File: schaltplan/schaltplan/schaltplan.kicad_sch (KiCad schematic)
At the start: 14 parts, among them SW1 SW_Nidec_CAS-120A1, U1 DFR0478

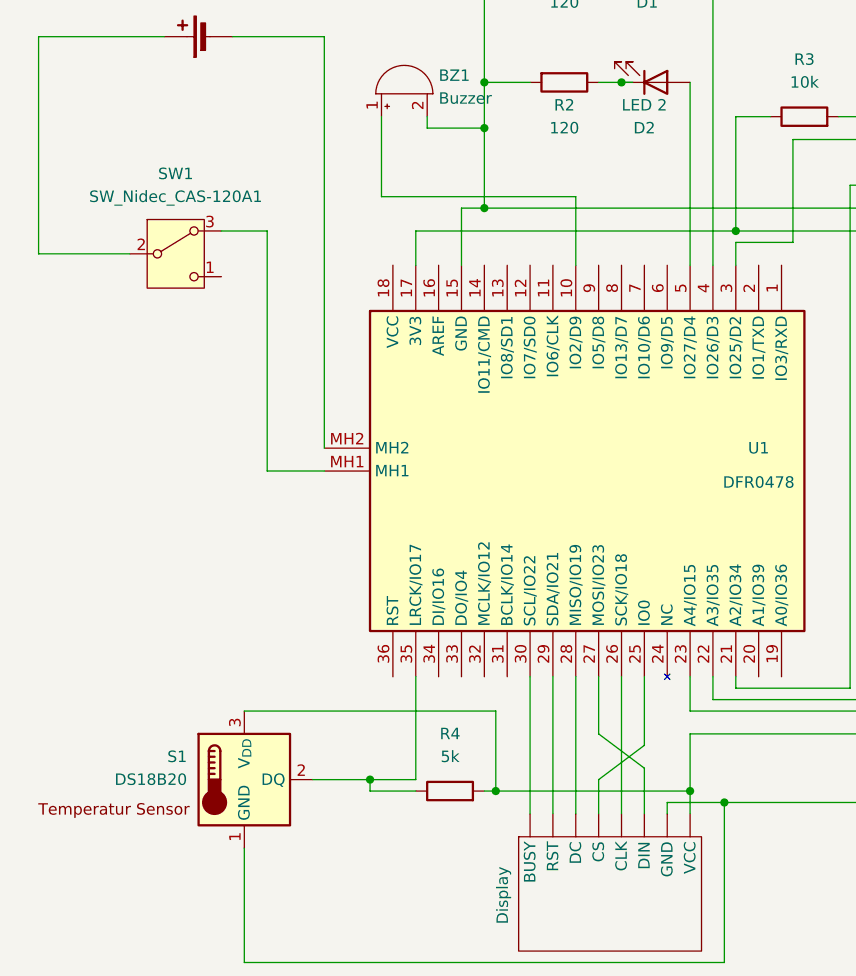
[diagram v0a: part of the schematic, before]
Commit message: schaltplan farbiger gemacht
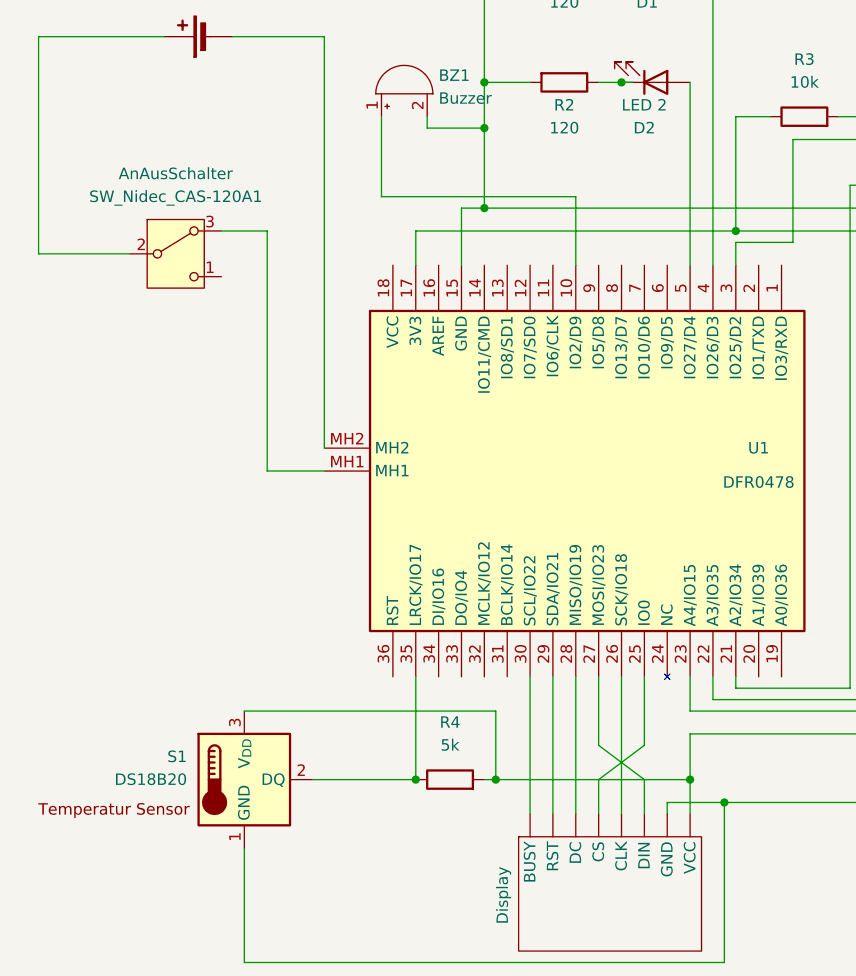
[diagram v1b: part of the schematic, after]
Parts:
- renumbered SW1 to AnAusSchalter
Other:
- moved on the sheet: R4
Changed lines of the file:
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@@
 	)
 	(junction
-		(at 90.17 134.62)
+		(at 68.58 133.35)
 		(diameter 0)
 		(color 0 0 0 0)
@@
 	)
 	(junction
+		(at 90.17 133.35)
+		(diameter 0)
+		(color 0 0 0 0)
+	)
+	(junction
 		(at 120.65 72.39)
 		(diameter 0)
@@
 	)
 	(junction
-		(at 93.98 135.89)
+		(at 59.69 133.35)
 		(diameter 0)
 		(color 0 0 0 0)
 	)
 	(junction
-		(at 54.61 133.35)
-		(diameter 0)
-		(color 0 0 0 0)
-	)
-	(junction
-		(at 68.58 134.62)
+		(at 93.98 135.89)
 		(diameter 0)
 		(color 0 0 0 0)
@@
 			(width 0)
 			(type default)
+			(color 255 255 255 1)
 		)
 	)
@@
 			(width 0)
 			(type default)
-		)
-	)
-	(wire
-		(pts
-			(xy 85.09 132.08) (xy 80.01 128.27)
-		)
-		(stroke
-			(width 0)
-			(type default)
+			(color 254 255 0 1)
+		)
+	)
+	(wire
+		(pts
+			(xy 85.09 133.35) (xy 80.01 129.54)
+		)
+		(stroke
+			(width 0)
+			(type default)
+			(color 0 45 255 1)
+		)
+	)
+	(wire
+		(pts
+			(xy 68.58 133.35) (xy 68.58 125.73)
+		)
+		(stroke
+			(width 0)
+			(type default)
+			(color 255 0 9 1)
 		)
 	)
@@
 			(width 0)
 			(type default)
+			(color 255 135 0 1)
 		)
 	)
@@
 			(width 0)
 			(type default)
+			(color 19 191 0 1)
 		)
 	)
@@
 			(width 0)
 			(type default)
+			(color 14 193 0 1)
 		)
 	)
@@
 			(width 0)
 			(type default)
+			(color 253 0 0 1)
 		)
 	)
@@
 	(wire
 		(pts
-			(xy 54.61 134.62) (xy 54.61 133.35)
-		)
-		(stroke
-			(width 0)
-			(type default)
-		)
-	)
-	(wire
-		(pts
 			(xy 80.01 137.16) (xy 80.01 133.35)
 		)
@@
 			(width 0)
 			(type default)
+			(color 255 135 0 1)
 		)
 	)
@@
 	(wire
 		(pts
-			(xy 67.31 134.62) (xy 68.58 134.62)
+			(xy 67.31 133.35) (xy 68.58 133.35)
 		)
 		(stroke
@@
 			(width 0)
 			(type default)
+			(color 0 0 0 1)
 		)
 	)
@@
 			(width 0)
 			(type default)
+			(color 255 255 255 1)
 		)
 	)
@@
 			(width 0)
 			(type default)
+			(color 0 0 0 1)
 		)
 	)
@@
 	(wire
 		(pts
-			(xy 80.01 128.27) (xy 80.01 121.92)
-		)
-		(stroke
-			(width 0)
-			(type default)
+			(xy 80.01 129.54) (xy 80.01 121.92)
+		)
+		(stroke
+			(width 0)
+			(type default)
+			(color 0 45 255 1)
 		)
 	)
@@
 			(width 0)
 			(type default)
+			(color 255 255 255 1)
 		)
 	)
@@
 			(width 0)
 			(type default)
+			(color 253 0 0 1)
 		)
 	)
@@
 			(width 0)
 			(type default)
+			(color 254 255 0 1)
 		)
 	)
@@
 	(wire
 		(pts
-			(xy 68.58 134.62) (xy 90.17 134.62)
-		)
-		(stroke
-			(width 0)
-			(type default)
-			(color 255 0 9 1)
-		)
-	)
-	(wire
-		(pts
 			(xy 87.63 135.89) (xy 87.63 137.16)
 		)
@@
 			(width 0)
 			(type default)
+			(color 144 0 0 1)
 		)
 	)
@@
 			(width 0)
 			(type default)
-			(color 0 0 0 1)
+			(color 144 0 0 1)
 		)
 	)
@@
 			(width 0)
 			(type default)
+			(color 19 191 0 1)
 		)
 	)
@@
 	(wire
 		(pts
-			(xy 59.69 133.35) (xy 54.61 133.35)
-		)
-		(stroke
-			(width 0)
-			(type default)
-		)
-	)
-	(wire
-		(pts
 			(xy 138.43 114.3) (xy 138.43 127)
 		)
@@
 			(width 0)
 			(type default)
+			(color 255 255 255 1)
 		)
 	)
@@
 	(wire
 		(pts
+			(xy 68.58 133.35) (xy 90.17 133.35)
+		)
+		(stroke
+			(width 0)
+			(type default)
+			(color 255 0 9 1)
+		)
+	)
+	(wire
+		(pts
 			(xy 95.25 73.66) (xy 95.25 76.2)
 		)
@@
 			(width 0)
 			(type default)
+			(color 249 0 0 1)
 		)
 	)
@@
 	(wire
 		(pts
-			(xy 90.17 134.62) (xy 90.17 137.16)
-		)
-		(stroke
-			(width 0)
-			(type default)
-			(color 255 0 9 1)
+			(xy 90.17 133.35) (xy 90.17 137.16)
+		)
+		(stroke
+			(width 0)
+			(type default)
+			(color 190 190 190 1)
 		)
 	)
@@
 			(width 0)
 			(type default)
-		)
-	)
-	(wire
-		(pts
-			(xy 90.17 128.27) (xy 90.17 134.62)
+			(color 140 0 255 1)
+		)
+	)
+	(wire
+		(pts
+			(xy 90.17 128.27) (xy 90.17 133.35)
 		)
 		(stroke
@@
 			(width 0)
 			(type default)
+			(color 249 0 0 1)
 		)
 	)
@@
 			(width 0)
 			(type default)
+			(color 255 255 255 1)
 		)
 	)
@@
 			(width 0)
 			(type default)
+			(color 255 135 0 1)
 		)
 	)
@@
 	(wire
 		(pts
-			(xy 85.09 132.08) (xy 85.09 137.16)
-		)
-		(stroke
-			(width 0)
-			(type default)
+			(xy 85.09 133.35) (xy 85.09 137.16)
+		)
+		(stroke
+			(width 0)
+			(type default)
+			(color 0 45 255 1)
 		)
 	)
@@
 			(width 0)
 			(type default)
-		)
-	)
-	(wire
-		(pts
-			(xy 68.58 134.62) (xy 68.58 125.73)
-		)
-		(stroke
-			(width 0)
-			(type default)
-			(color 255 0 9 1)
+			(color 254 255 0 1)
 		)
 	)
@@
 			(width 0)
 			(type default)
+			(color 255 255 0 1)
 		)
 	)
@@
 			(width 0)
 			(type default)
+			(color 254 255 0 1)
 		)
 	)
@@
 	(wire
 		(pts
-			(xy 59.69 134.62) (xy 54.61 134.62)
-		)
-		(stroke
-			(width 0)
-			(type default)
-		)
-	)
-	(wire
-		(pts
 			(xy 120.65 135.89) (xy 93.98 135.89)
 		)
@@
 			(width 0)
 			(type default)
+			(color 19 191 0 1)
 		)
 	)
@@
 			(width 0)
 			(type default)
-		)
-	)
-	(wire
-		(pts
-			(xy 54.61 133.35) (xy 48.26 133.35)
+			(color 253 0 0 1)
+		)
+	)
+	(wire
+		(pts
+			(xy 48.26 133.35) (xy 59.69 133.35)
 		)
 		(stroke
@@
 			(width 0)
 			(type default)
+			(color 249 0 0 1)
 		)
 	)
@@
 		(dnp no)
 		(fields_autoplaced yes)
-		(property "Reference" "SW1"
+		(property "Reference" "AnAusSchalter"
 			(at 33.02 66.04 0)
 			(effects
@@
 			(project ""
 				(path "/f79f94d7-572e-4250-b494-96d40f946eb3"
-					(reference "SW1")
+					(reference "AnAusSchalter")
 					(unit 1)
 				)
@@
 	(symbol
 		(lib_id "Device:R")
-		(at 63.5 134.62 90)
+		(at 63.5 133.35 90)
 		(unit 1)
 		(exclude_from_sim no)
@@
 		(fields_autoplaced yes)
 		(property "Reference" "R4"
-			(at 63.5 128.27 90)
+			(at 63.5 127 90)
 			(effects
 				(font
@@
 		)
 		(property "Value" "5k"
-			(at 63.5 130.81 90)
+			(at 63.5 129.54 90)
 			(effects
 				(font
@@
 		)
 		(property "Footprint" ""
-			(at 63.5 136.398 90)
+			(at 63.5 135.128 90)
 			(effects
 				(font
@@
 		)
 		(property "Datasheet" "~"
-			(at 63.5 134.62 0)
+			(at 63.5 133.35 0)
 			(effects
 				(font
@@
 		)
 		(property "Description" "Resistor"
-			(at 63.5 134.62 0)
-			(effects
-				(font
+			(at 63.5 133.35 0)
+			(effects
+				(font

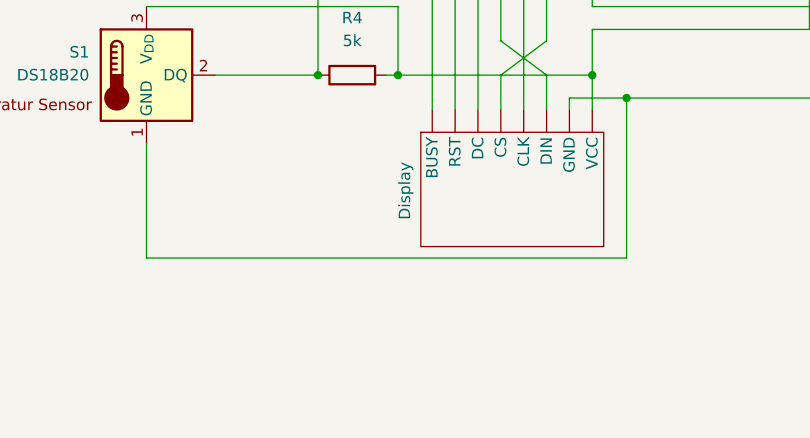
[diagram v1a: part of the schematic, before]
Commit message: Schaltplan geändert
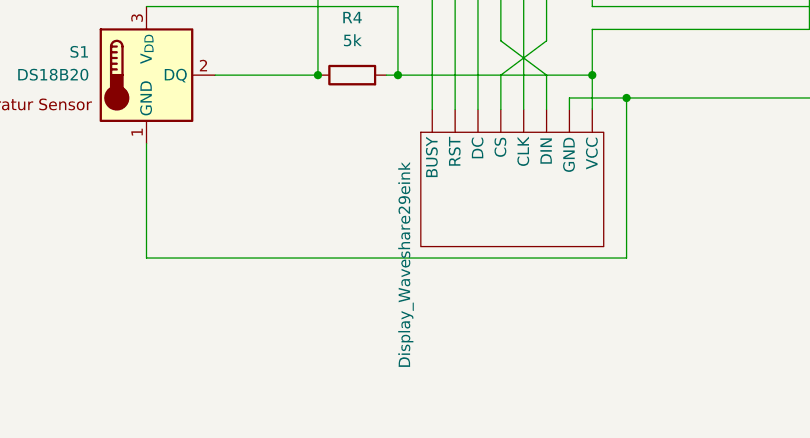
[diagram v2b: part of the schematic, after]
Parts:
- renumbered Display to Display_Waveshare29eink
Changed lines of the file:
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@@
 		(on_board yes)
 		(dnp no)
-		(property "Reference" "Display"
+		(property "Reference" "Display_Waveshare29eink"
 			(at 69.342 143.002 0)
 			(effects
@@
 			(project ""
 				(path "/f79f94d7-572e-4250-b494-96d40f946eb3"
-					(reference "Display")
+					(reference "Display_Waveshare29eink")
 					(unit 1)
 				)

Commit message: bezeichnungen angepasst
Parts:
- Display: renamed from Display_Waveshare29eink; value ~ -> Waveshare 29 E-Ink
- Schalter: renamed from AnAusSchalter; value SW_Nidec_CAS-120A1 -> An/Aus Switch
- renumbered U1 to ESP, S1 to TS1
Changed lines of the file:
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@@
 		(dnp no)
 		(fields_autoplaced yes)
-		(property "Reference" "AnAusSchalter"
+		(property "Reference" "Schalter"
 			(at 33.02 66.04 0)
 			(effects
@@
 			)
 		)
-		(property "Value" "SW_Nidec_CAS-120A1"
+		(property "Value" "An/Aus Switch"
 			(at 33.02 68.58 0)
 			(effects
@@
 			(project ""
 				(path "/f79f94d7-572e-4250-b494-96d40f946eb3"
-					(reference "AnAusSchalter")
+					(reference "Schalter")
 					(unit 1)
 				)
@@
 		(on_board yes)
 		(dnp no)
-		(property "Reference" "Display_Waveshare29eink"
-			(at 69.342 143.002 0)
+		(property "Reference" "Display"
+			(at 69.85 144.78 90)
 			(effects
 				(font
@@
 			)
 		)
-		(property "Value" "~"
+		(property "Value" "Waveshare 29 E-Ink"
 			(at 69.85 147.32 90)
 			(effects
@@
 			(project ""
 				(path "/f79f94d7-572e-4250-b494-96d40f946eb3"
-					(reference "Display_Waveshare29eink")
+					(reference "Display")
 					(unit 1)
 				)
@@
 		(on_board yes)
 		(dnp no)
-		(property "Reference" "S1"
+		(property "Reference" "TS1"
 			(at 34.29 130.81 0)
 			(effects
@@
 			(project ""
 				(path "/f79f94d7-572e-4250-b494-96d40f946eb3"
-					(reference "S1")
+					(reference "TS1")
 					(unit 1)
 				)
@@
 		(on_board yes)
 		(dnp no)
-		(property "Reference" "U1"
+		(property "Reference" "ESP"
 			(at 97.79 96.52 0)
 			(effects
@@
 			(project ""
 				(path "/f79f94d7-572e-4250-b494-96d40f946eb3"
-					(reference "U1")
+					(reference "ESP")
 					(unit 1)
 				)

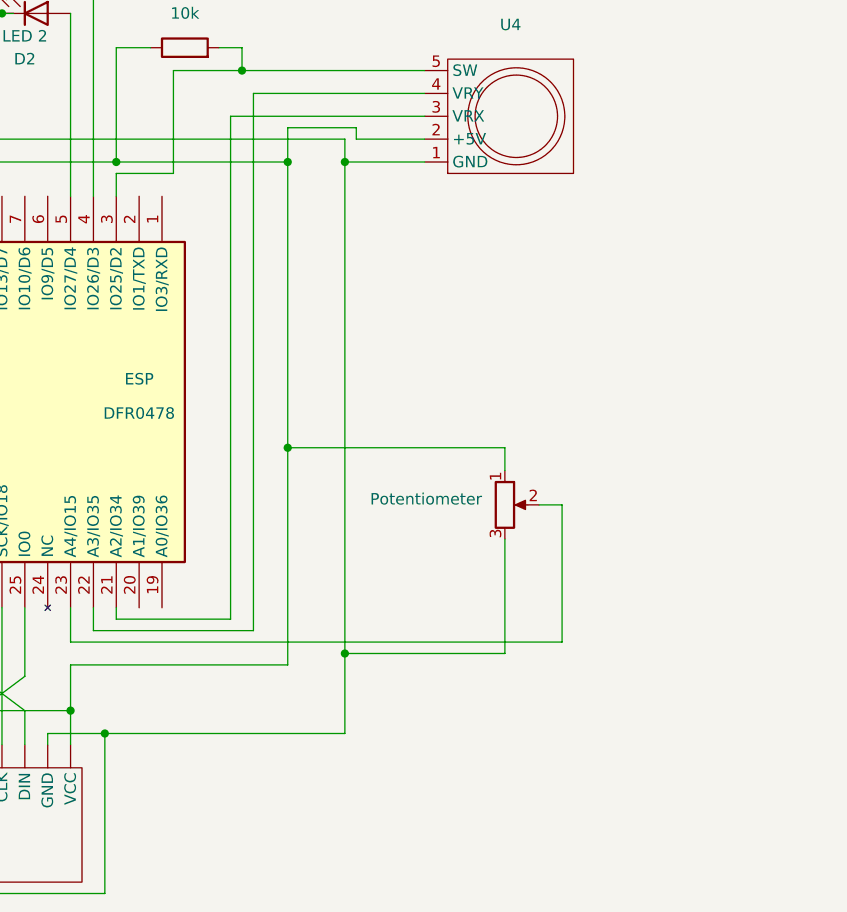
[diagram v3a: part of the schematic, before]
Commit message: buttonarray eingezeichnet mit diversen vorwiderständen sowie 100k pull down auf ground
im setup wird die melodie nur einmal beim start gespielt (aber noch immer falsch!)
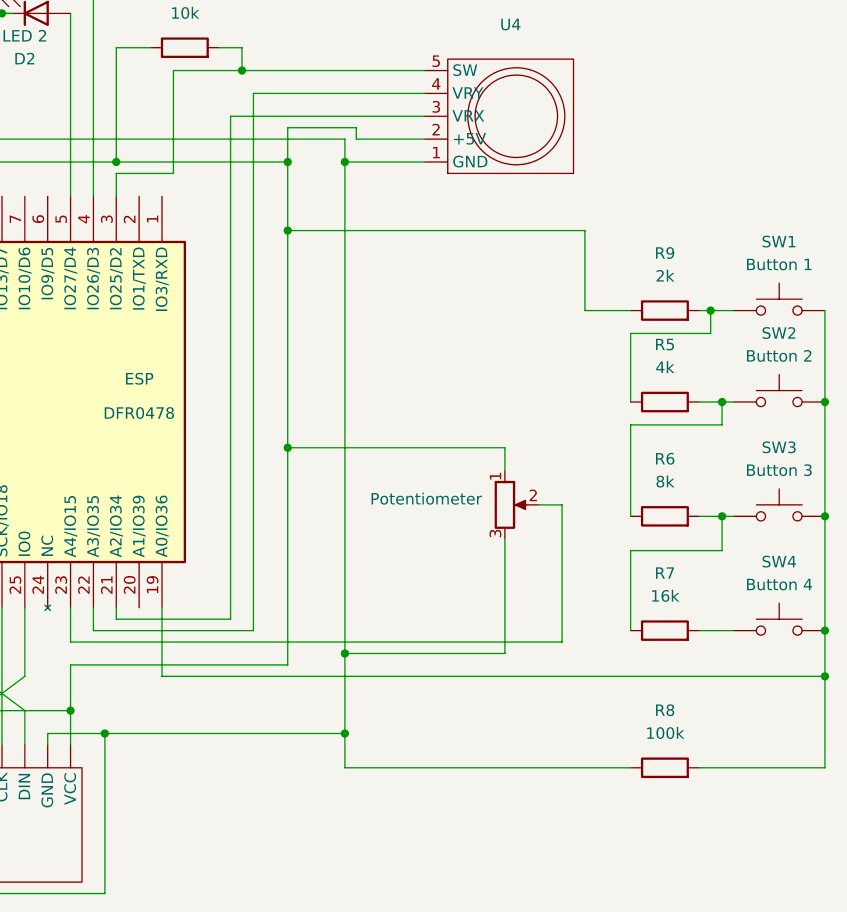
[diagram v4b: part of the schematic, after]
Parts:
- added R5: 4k, symbol Device:R
- added R6: 8k, symbol Device:R
- added R7: 16k, symbol Device:R
- added R8: 100k, symbol Device:R
- added R9: 2k, symbol Device:R
- added SW1: Button 1, symbol Switch:SW_Push
- added SW2: Button 2, symbol Switch:SW_Push
- added SW3: Button 3, symbol Switch:SW_Push
- added SW4: Button 4, symbol Switch:SW_Push
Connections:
- net at BZ1.2 (-), Display. (VCC), ESP.15 (GND)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: now also R8.1
- net at Display. (VCC), ESP.17 (3V3), Potentiometer.1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: now also R9.1
- net at ESP.19 (A0/IO36): now also R8.2, SW1.2, SW2.2, SW3.2, SW4.2
- new net: R6.2, R7.1, SW3.1
- new net: R5.2, R6.1, SW2.1
- new net: R5.1, R9.2, SW1.1
- new net: R7.2, SW4.1

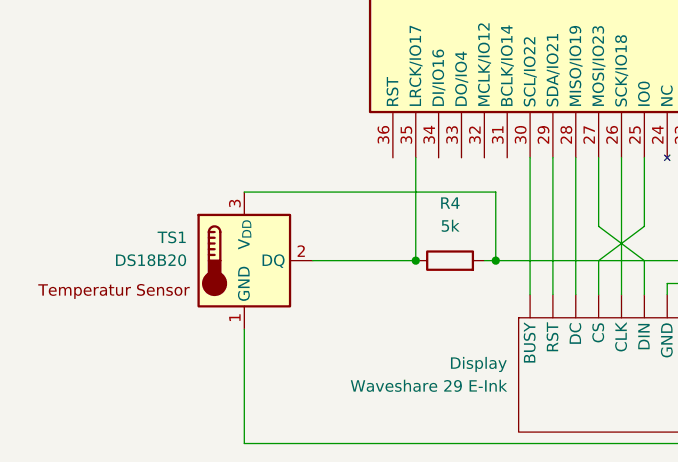
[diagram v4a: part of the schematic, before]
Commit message: orientierung des temperatursensors eingefügt
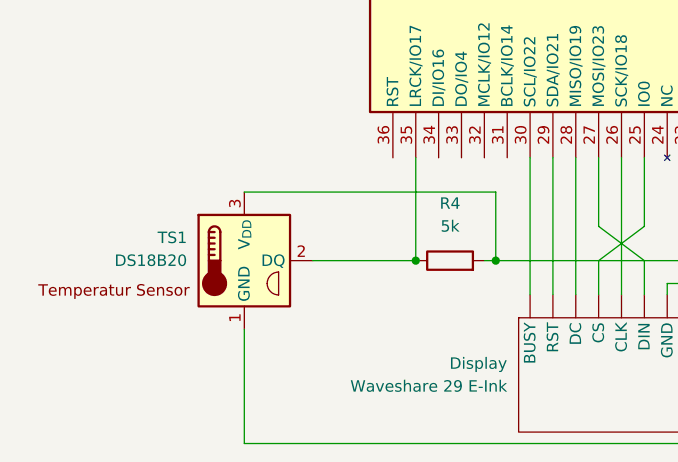
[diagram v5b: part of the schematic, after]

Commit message: schaltplan aktualisiert mit da wandler für buttons
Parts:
- removed R7: 16k, symbol Device:R
- added R10, R6: 1k, symbol Device:R
- added R11, R12: 2k, symbol Device:R
- R5: value 4k -> 2k
- R7: renamed from R6; value 8k -> 2k
- R8: value 100k -> 1k
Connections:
- net at BZ1.2 (-), Display. (VCC), ESP.15 (GND)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: now also R12.2; no longer R8.1
- net at SW3.1: now also Display. (VCC), ESP.17 (3V3), Potentiometer.1, R3.1, R4.2, SW1.1, SW2.1, SW4.1, TS1.3 (V_{DD}), U4.2 (+5V); no longer R7.2
- new net: R9.1, SW3.2
- new net: R7.1, SW2.2
- new net: R5.1, SW1.2
- new net: R6.1, R7.2, R8.2
- new net: ESP.19 (A0/IO36), R5.2, R6.2
- new net: R10.1, R11.2, R12.1
- new net: R10.2, R8.1, R9.2
- new net: R11.1, SW4.2
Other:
- moved on the sheet: R5, R7, R9, SW1, SW2, SW3, SW4
